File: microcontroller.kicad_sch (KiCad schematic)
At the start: 20 parts, among them J3 USART1 Header, J4 I2C1 Header, J5 SPI Header, J6 SWD Header, SW1 Boot Switch, SW2 System Reset, U2 STM32F401RETx, Y1 16MHz

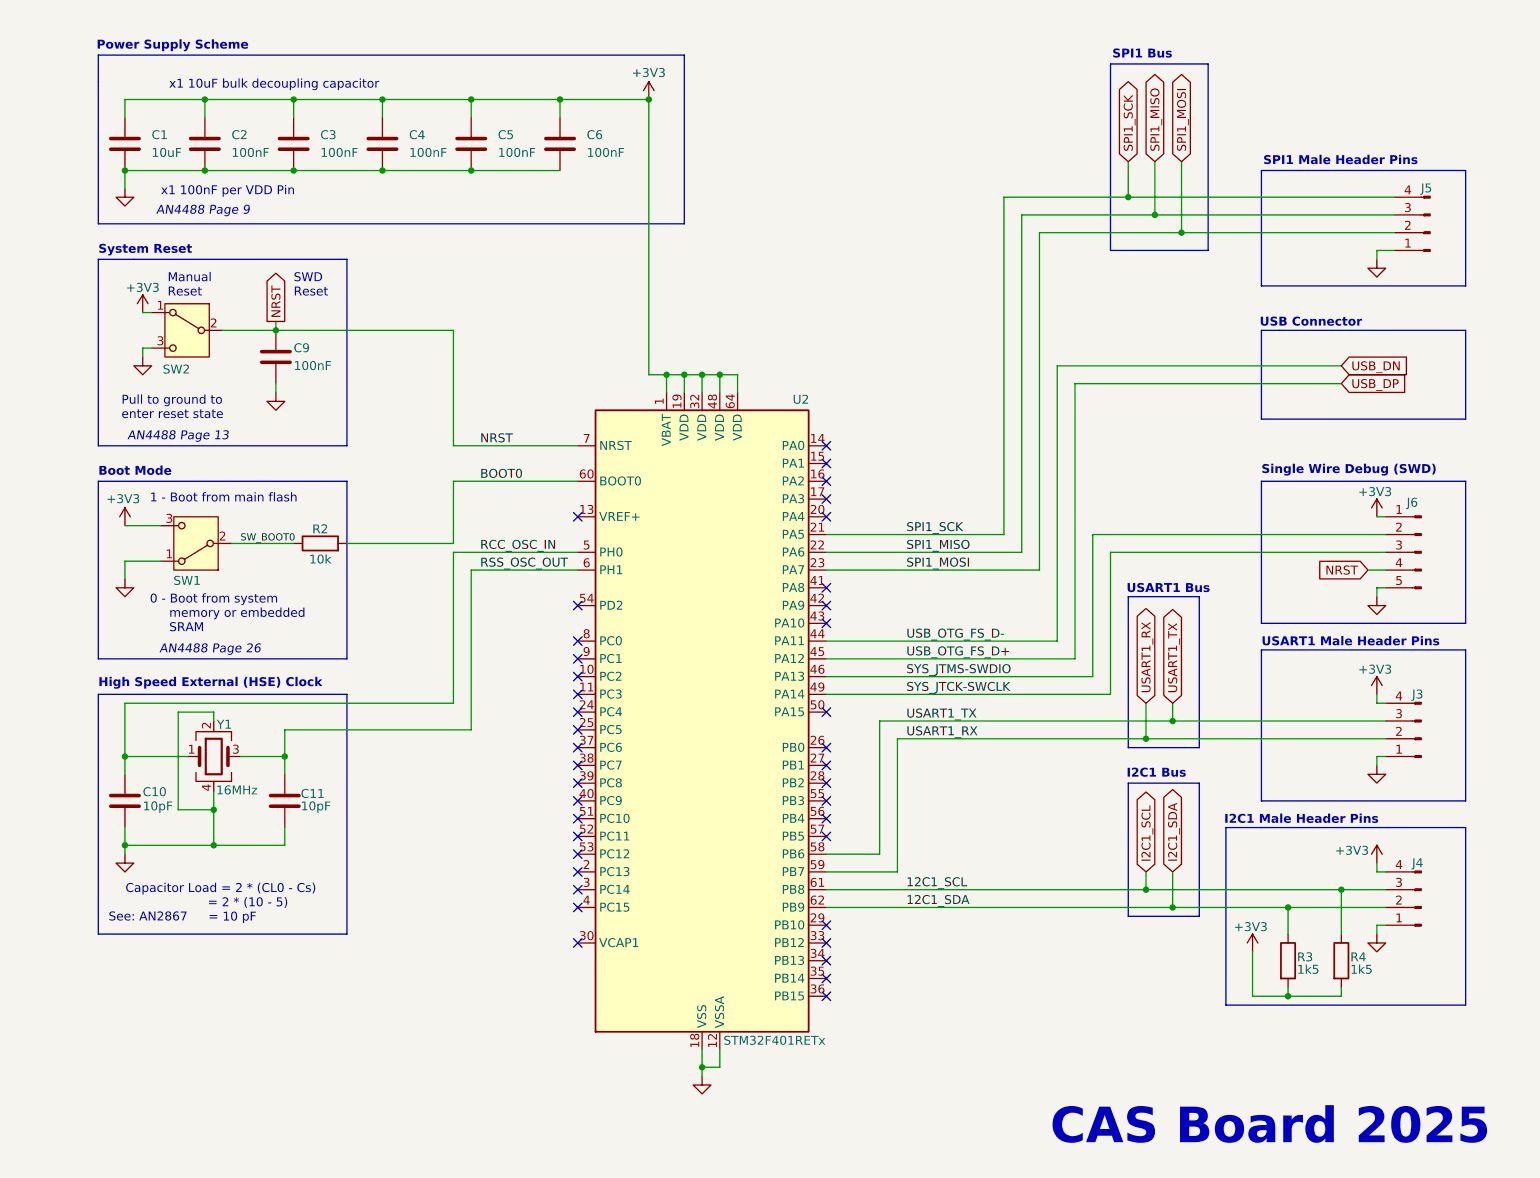
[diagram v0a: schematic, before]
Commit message: Use heirarchical labels
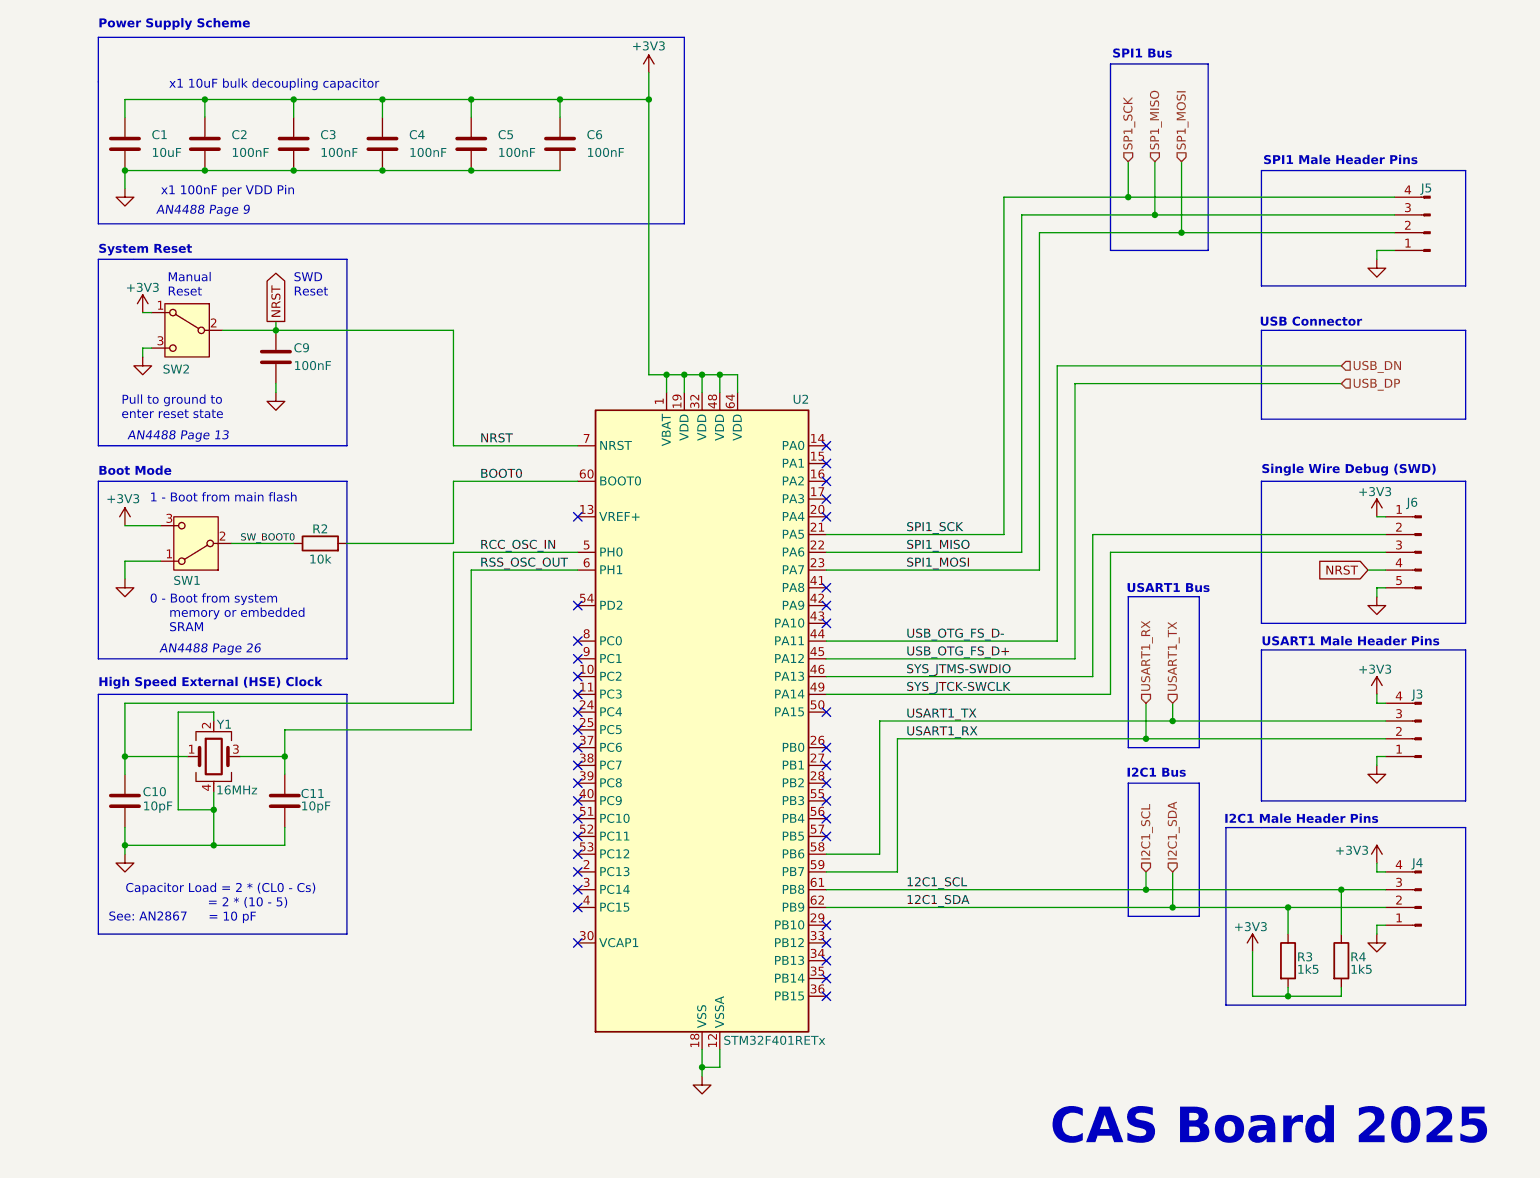
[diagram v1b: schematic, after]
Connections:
- net SPI1_MISO renamed SP1_MISO
- net SPI1_MOSI renamed SP1_MOSI
- net SPI1_SCK renamed SP1_SCK
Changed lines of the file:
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@@
 	(text "Power Supply Scheme"
 		(exclude_from_sim no)
-		(at 41.656 19.05 0)
+		(at 41.91 16.002 0)
 		(effects
 			(font
@@
 		)
 	)
+	(wire
+		(pts
+			(xy 173.99 43.18) (xy 193.04 43.18)
+		)
+		(stroke
+			(width 0)
+			(type default)
+		)
+	)
 	(polyline
 		(pts
@@
 	(polyline
 		(pts
-			(xy 41.91 20.32) (xy 125.73 20.32)
+			(xy 41.91 17.78) (xy 125.73 17.78)
 		)
 		(stroke
@@
 	(polyline
 		(pts
-			(xy 41.91 24.13) (xy 41.91 20.32)
+			(xy 41.91 24.13) (xy 41.91 17.78)
 		)
 		(stroke
@@
 	(wire
 		(pts
-			(xy 173.99 43.18) (xy 193.04 43.18)
-		)
-		(stroke
-			(width 0)
-			(type default)
-		)
-	)
-	(wire
-		(pts
 			(xy 45.72 95.25) (xy 45.72 92.71)
 		)
@@
 	(polyline
 		(pts
-			(xy 125.73 20.32) (xy 125.73 44.45)
+			(xy 125.73 17.78) (xy 125.73 44.45)
 		)
 		(stroke
@@
 	(wire
 		(pts
+			(xy 120.65 22.86) (xy 120.65 26.67)
+		)
+		(stroke
+			(width 0)
+			(type default)
+		)
+	)
+	(wire
+		(pts
 			(xy 219.71 139.7) (xy 226.06 139.7)
 		)
@@
 		)
 	)
-	(global_label "USART1_RX"
-		(shape bidirectional)
-		(at 191.77 113.03 90)
+	(global_label "NRST"
+		(shape input)
+		(at 223.52 93.98 180)
 		(fields_autoplaced yes)
 		(effects
@@
 				(size 1.27 1.27)
 			)
-			(justify left)
+			(justify right)
 		)
 		(property "Intersheetrefs" "${INTERSHEET_REFS}"
-			(at 191.77 98.4107 90)
+			(at 215.7572 93.98 0)
 			(effects
 				(font
 					(size 1.27 1.27)
 				)
-				(justify left)
+				(justify right)
 			)
 		)
 	)
-	(global_label "USART1_TX"
-		(shape bidirectional)
-		(at 195.58 113.03 90)
+	(global_label "NRST"
+		(shape output)
+		(at 67.31 58.42 90)
 		(fields_autoplaced yes)
 		(effects
@@
 		)
 		(property "Intersheetrefs" "${INTERSHEET_REFS}"
-			(at 195.58 98.7131 90)
+			(at 67.31 50.6572 90)
 			(effects
 				(font
@@
 		)
 	)
-	(global_label "SPI1_SCK"
-		(shape bidirectional)
+	(hierarchical_label "SP1_SCK"
+		(shape input)
 		(at 189.23 35.56 90)
-		(fields_autoplaced yes)
 		(effects
 			(font
@@
 			(justify left)
 		)
-		(property "Intersheetrefs" "${INTERSHEET_REFS}"
-			(at 189.23 22.4526 90)
-			(effects
-				(font
-					(size 1.27 1.27)
-				)
-				(justify left)
-			)
-		)
 	)
-	(global_label "NRST"
+	(hierarchical_label "I2C1_SCL"
 		(shape input)
-		(at 223.52 93.98 180)
-		(fields_autoplaced yes)
+		(at 191.77 137.16 90)
 		(effects
 			(font
 				(size 1.27 1.27)
 			)
-			(justify right)
-		)
-		(property "Intersheetrefs" "${INTERSHEET_REFS}"
-			(at 215.7572 93.98 0)
-			(effects
-				(font
-					(size 1.27 1.27)
-				)
-				(justify right)
-			)
+			(justify left)
 		)
 	)
-	(global_label "NRST"
-		(shape output)
-		(at 67.31 58.42 90)
-		(fields_autoplaced yes)
+	(hierarchical_label "USB_DP"
+		(shape input)
+		(at 219.71 67.31 0)
 		(effects
 			(font
@@
 			(justify left)
 		)
-		(property "Intersheetrefs" "${INTERSHEET_REFS}"
-			(at 67.31 50.6572 90)
-			(effects
-				(font
-					(size 1.27 1.27)
-				)
-				(justify left)
-			)
-		)
 	)
-	(global_label "I2C1_SCL"
-		(shape bidirectional)
-		(at 191.77 137.16 90)
-		(fields_autoplaced yes)
+	(hierarchical_label "SP1_MOSI"
+		(shape input)
+		(at 196.85 35.56 90)
 		(effects
 			(font
@@
 			(justify left)
 		)
-		(property "Intersheetrefs" "${INTERSHEET_REFS}"
-			(at 191.77 124.2945 90)
-			(effects
-				(font
-					(size 1.27 1.27)
-				)
-				(justify left)
-			)
-		)
 	)
-	(global_label "USB_DP"
+	(hierarchical_label "I2C1_SDA"
 		(shape input)
-		(at 219.71 67.31 0)
-		(fields_autoplaced yes)
+		(at 195.58 137.16 90)
 		(effects
 			(font
@@
 			(justify left)
 		)
-		(property "Intersheetrefs" "${INTERSHEET_REFS}"
-			(at 230.0128 67.31 0)
-			(effects
-				(font
-					(size 1.27 1.27)
-				)
-				(justify left)
-			)
-		)
 	)
-	(global_label "I2C1_SDA"
-		(shape bidirectional)
-		(at 195.58 137.16 90)
-		(fields_autoplaced yes)
+	(hierarchical_label "SP1_MISO"
+		(shape input)
+		(at 193.04 35.56 90)
 		(effects
 			(font
@@
 			(justify left)
 		)
-		(property "Intersheetrefs" "${INTERSHEET_REFS}"
-			(at 195.58 124.234 90)
-			(effects
-				(font
-					(size 1.27 1.27)
-				)
-				(justify left)
-			)
-		)
 	)
-	(global_label "SPI1_MOSI"
-		(shape bidirectional)
-		(at 196.85 35.56 90)
-		(fields_autoplaced yes)
+	(hierarchical_label "USART1_TX"
+		(shape input)
+		(at 195.58 113.03 90)
 		(effects
 			(font
@@
 			(justify left)
 		)
-		(property "Intersheetrefs" "${INTERSHEET_REFS}"
-			(at 196.85 21.6059 90)
-			(effects
-				(font
-					(size 1.27 1.27)
-				)
-				(justify left)
-			)
-		)
 	)
-	(global_label "SPI1_MISO"
-		(shape bidirectional)
-		(at 193.04 35.56 90)
-		(fields_autoplaced yes)
+	(hierarchical_label "USART1_RX"
+		(shape input)
+		(at 191.77 113.03 90)
 		(effects
 			(font
@@
 			(justify left)
 		)
-		(property "Intersheetrefs" "${INTERSHEET_REFS}"
-			(at 193.04 21.6059 90)
-			(effects
-				(font
-					(size 1.27 1.27)
-				)
-				(justify left)
-			)
-		)
 	)
-	(global_label "USB_DN"
+	(hierarchical_label "USB_DN"
 		(shape input)
 		(at 219.71 64.77 0)
-		(fields_autoplaced yes)
 		(effects
 			(font
@@
 			(justify left)
 		)
-		(property "Intersheetrefs" "${INTERSHEET_REFS}"
-			(at 230.0733 64.77 0)
-			(effects
-				(font
-					(size 1.27 1.27)
-				)
-				(justify left)
-			)
-		)
 	)
 	(symbol
@@
 	(symbol
 		(lib_id "power:+3V3")
-		(at 120.65 26.67 0)
+		(at 120.65 22.86 0)
 		(unit 1)
 		(exclude_from_sim no)
@@
 		(dnp no)
 		(property "Reference" "#PWR01"
-			(at 120.65 30.48 0)
+			(at 120.65 26.67 0)
 			(effects
 				(font
@@
 		)
 		(property "Value" "+3V3"
-			(at 120.65 22.86 0)
+			(at 120.65 19.05 0)
 			(effects
 				(font
@@
 		)
 		(property "Footprint" ""
-			(at 120.65 26.67 0)
+			(at 120.65 22.86 0)
 			(effects
 				(font
@@
 		)
 		(property "Datasheet" ""
-			(at 120.65 26.67 0)
+			(at 120.65 22.86 0)
 			(effects
 				(font
@@
 		)
 		(property "Description" "Power symbol creates a global label with name \"+3V3\""
-			(at 120.65 26.67 0)
+			(at 120.65 22.86 0)
 			(effects
 				(font

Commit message: Broke headers into own heiarchicial sheet
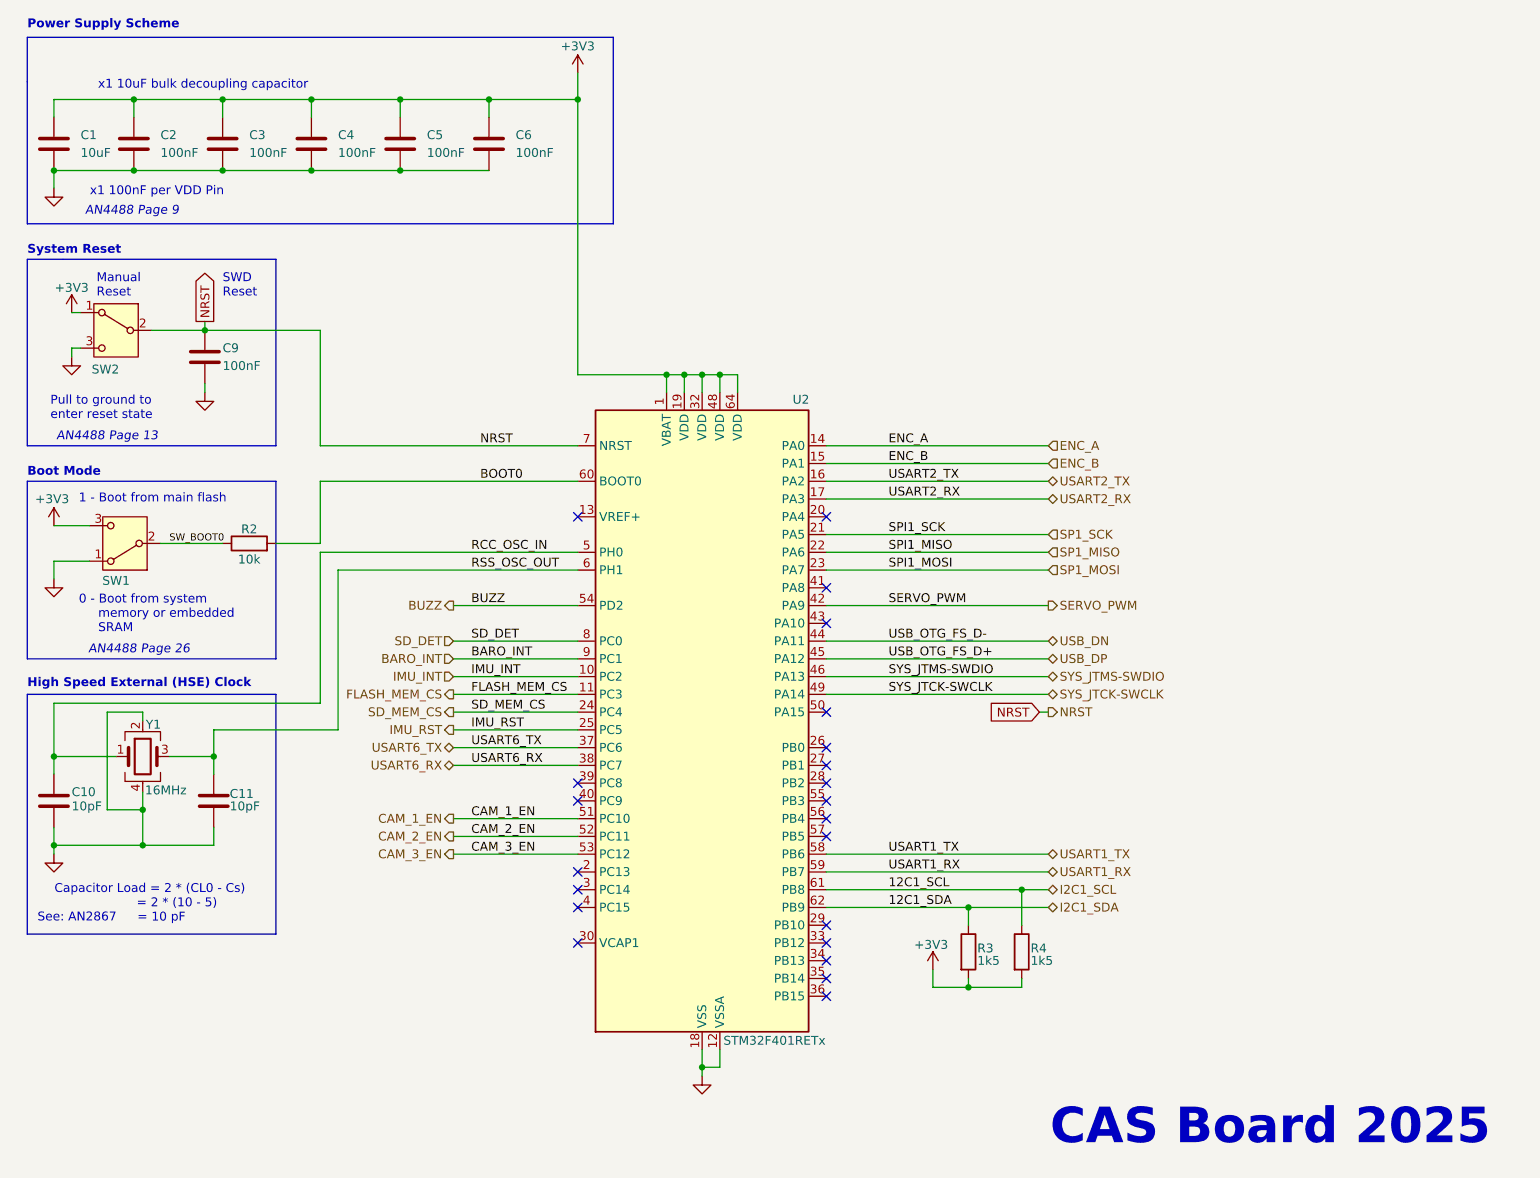
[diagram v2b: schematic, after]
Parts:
- removed J3: USART1 Header, Connector_PinHeader_2.54mm:PinHeader_1x04_P2.54mm_Vertical, symbol Connector:Conn_01x04_Pin
- removed J4: I2C1 Header, Connector_PinHeader_2.54mm:PinHeader_1x04_P2.54mm_Vertical, symbol Connector:Conn_01x04_Pin
- removed J5: SPI Header, Connector_PinHeader_2.54mm:PinHeader_1x04_P2.54mm_Vertical, symbol Connector:Conn_01x04_Pin
- removed J6: SWD Header, Connector_PinHeader_2.54mm:PinHeader_1x05_P2.54mm_Vertical, symbol Connector:Conn_01x05_Pin
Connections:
- net IMU_INT: now reaches U2.10 (PC2)
- net FLASH_MEM_CS: now reaches U2.11 (PC3)
- net ENC_A: now reaches U2.14 (PA0)
- net ENC_B: now reaches U2.15 (PA1)
- net USART2_TX: now reaches U2.16 (PA2)
- net USART2_RX: now reaches U2.17 (PA3)
- net SD_MEM_CS: now reaches U2.24 (PC4)
- net IMU_RST: now reaches U2.25 (PC5)
- net USART6_TX: now reaches U2.37 (PC6)
- net USART6_RX: now reaches U2.38 (PC7)
- net SERVO_PWM: now reaches U2.42 (PA9)
- net CAM_1_EN: now reaches U2.51 (PC10)
- net CAM_2_EN: now reaches U2.52 (PC11)
- net CAM_3_EN: now reaches U2.53 (PC12)
- net BUZZ: now reaches U2.54 (PD2)
- net SD_DET: now reaches U2.8 (PC0)
- net BARO_INT: now reaches U2.9 (PC1)
- no-connect marks 39 -> 22
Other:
- note removed: "I2C1 Bus"
- note removed: "I2C1 Male Header Pins"
- note removed: "SPI1 Bus"
- note removed: "SPI1 Male Header Pins"
- note removed: "Single Wire Debug (SWD)"
- note removed: "USART1 Bus"
- note removed: "USART1 Male Header Pins"
- note removed: "USB Connector"
- moved on the sheet: C1, C10, C11, C2, C3, C4, C5, C6, C9, R2, R3, R4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

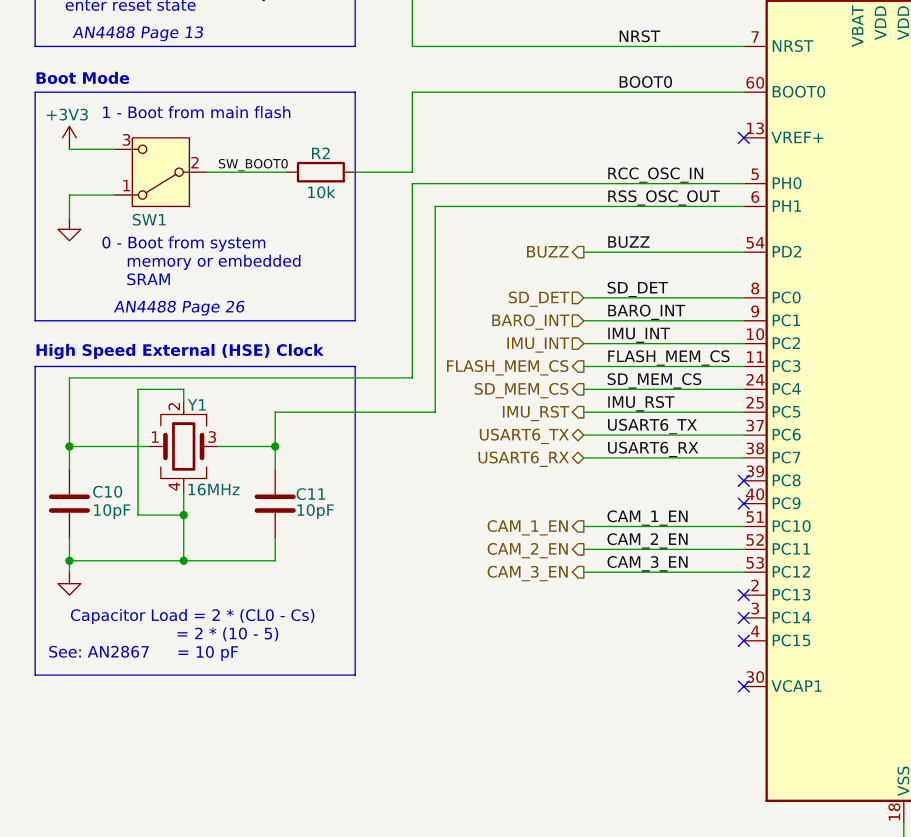
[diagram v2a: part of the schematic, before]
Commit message: Removed external highspeed clock
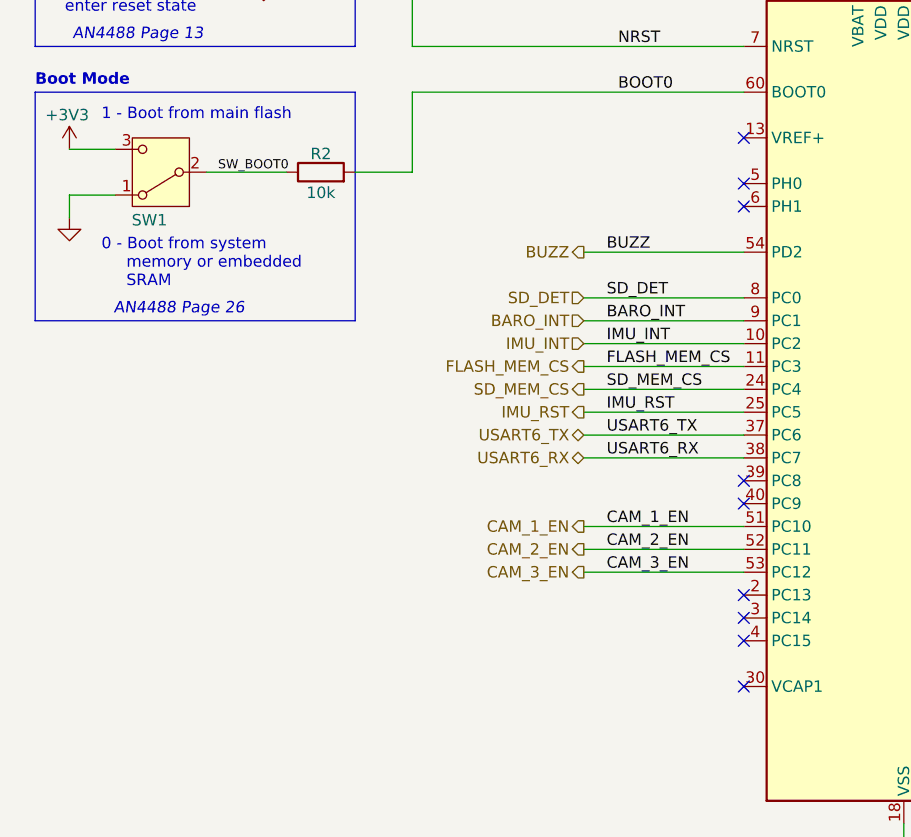
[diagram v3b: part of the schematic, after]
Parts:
- removed C10, C11: 10pF, Capacitor_SMD:C_0805_2012Metric, symbol Device:C
- removed Y1: 16MHz, Crystal:Crystal_SMD_3225-4Pin_3.2x2.5mm, symbol Device:Crystal_GND24
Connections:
- net RCC_OSC_IN: no longer names the net of U2.5 (PH0)
- net RSS_OSC_OUT: no longer names the net of U2.6 (PH1)
- no-connect marks 22 -> 24
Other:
- note removed: "Capacitor Load = 2 * (CL0 - Cs) = 2 * (10 - 5) = 10 pF"
- note removed: "High Speed External (HSE) Clock"
- note removed: "See: AN2867"
